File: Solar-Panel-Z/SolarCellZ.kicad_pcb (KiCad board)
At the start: 6 copper layers, 74.1 x 48.4 mm, 62 parts, among them IC1 TSL2561, J1 XF2M-1015-1A, Q1 IRLML2803, U1 NDS8434, U2 Value, U3 Value

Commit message: Finished Cleanup
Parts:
- removed IC1: TSL2561, misc-circuits:TSL2561
- added R17: 0, Resistor_SMD:R_0402_1005Metric, B.Cu at (109.3, 73.9)
- added R18: 0, Resistor_SMD:R_0402_1005Metric, B.Cu at (109.3, 75.8)
- added Ref**: Val**, custom-footprints:ypanel, F.Cu at (118.8, 74.9)
- added TP1: TP, TestPoint:TestPoint_THTPad_D1.0mm_Drill0.5mm, B.Cu at (114.1, 55.3)
- added TP2: TP, TestPoint:TestPoint_THTPad_D1.0mm_Drill0.5mm, B.Cu at (107.9, 55.3)
- added TP3: TP, TestPoint:TestPoint_THTPad_D1.0mm_Drill0.5mm, B.Cu at (110.9, 55.3)
- added TP4: TP, TestPoint:TestPoint_THTPad_D1.0mm_Drill0.5mm, B.Cu at (120.1, 55.3)
- added TP5: TP, TestPoint:TestPoint_THTPad_D1.0mm_Drill0.5mm, B.Cu at (117.3, 55.3)
- D4, D5, R12, R13: moved to B.Cu
- moved D4 58.7 mm to (99.4, 74.1), turned to 0 degrees
- moved R1 57.5 mm to (95.9, 59.3), turned to 180 degrees
- moved D5 56.9 mm to (95.6, 70.2), turned to -90 degrees
- moved C1 56.8 mm to (96.9, 60.3), turned to 180 degrees
- moved R2 55.9 mm to (97.8, 59.3)
- moved SC8 47.7 mm to (85.5, 82.6)
- moved R13 47.5 mm to (108.1, 73.9), turned to -90 degrees
- moved R12 47.3 mm to (108.1, 75.8), turned to -90 degrees
- moved SC2 45.6 mm to (109.6, 45.8), turned to 0 degrees
- moved D3 36.5 mm to (116.3, 72.1), turned to -90 degrees
- moved SC5 30.3 mm to (85.5, 64.2)
- moved SC7 27.0 mm to (85.5, 45.8), turned to 0 degrees
- moved SC6 25.0 mm to (92.8, 73.2)
- moved SC3 18.6 mm to (103.9, 55.2)
- moved SC4 18.1 mm to (109.6, 64.2)
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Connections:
- net /VSOLAR_FULL renamed VSOLAR_FULL
- JP1 pad 1: /coil -> /VBURN
- SC4 pad 1: /coil -> Net-(D3-Pad1)
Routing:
- net VSOLAR_FULL: track 3.25 -> 102.2 mm, vias 0 -> 3
- net Net-(D3-Pad1): track 0.00 -> 72.8 mm, vias 0 -> 4
- net GND: track 6.82 -> 74.2 mm, vias 2 -> 4
- net +3V3: track 2.75 -> 43.8 mm, vias 0 -> 3
- net BATT_P: track 3.63 -> 21.9 mm, vias 0 -> 2
- net SDA1: track 1.09 -> 19.2 mm, vias 1 -> 2
- net SCL1: track 1.13 -> 17.8 mm, vias 1 -> 2
- net /coil: track 15702.4 -> 15688.6 mm, vias 8 -> 7
- net Net-(R10-Pad2): track 3.74 -> 9.89 mm, vias 1 -> 2
- net BURN1: track 22.5 -> 28.3 mm
- net COIL_N: track 15.1 -> 20.1 mm, vias 1 -> 2
- net /VBAT: track 16.1 -> 13.4 mm, vias 3 -> 2
- net Net-(R1-Pad1): track 1.80 -> 4.22 mm
- net VSOLAR: track 1.63 -> 3.99 mm
- net COIL_P: track 17.4 -> 19.6 mm, vias 3 -> 2
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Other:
- board size 74.1 x 48.4 mm -> 48.4 x 48.4 mm
- board text added: "SOLAR_OUT"
- board text added: "v03"
- board text removed: "v02"

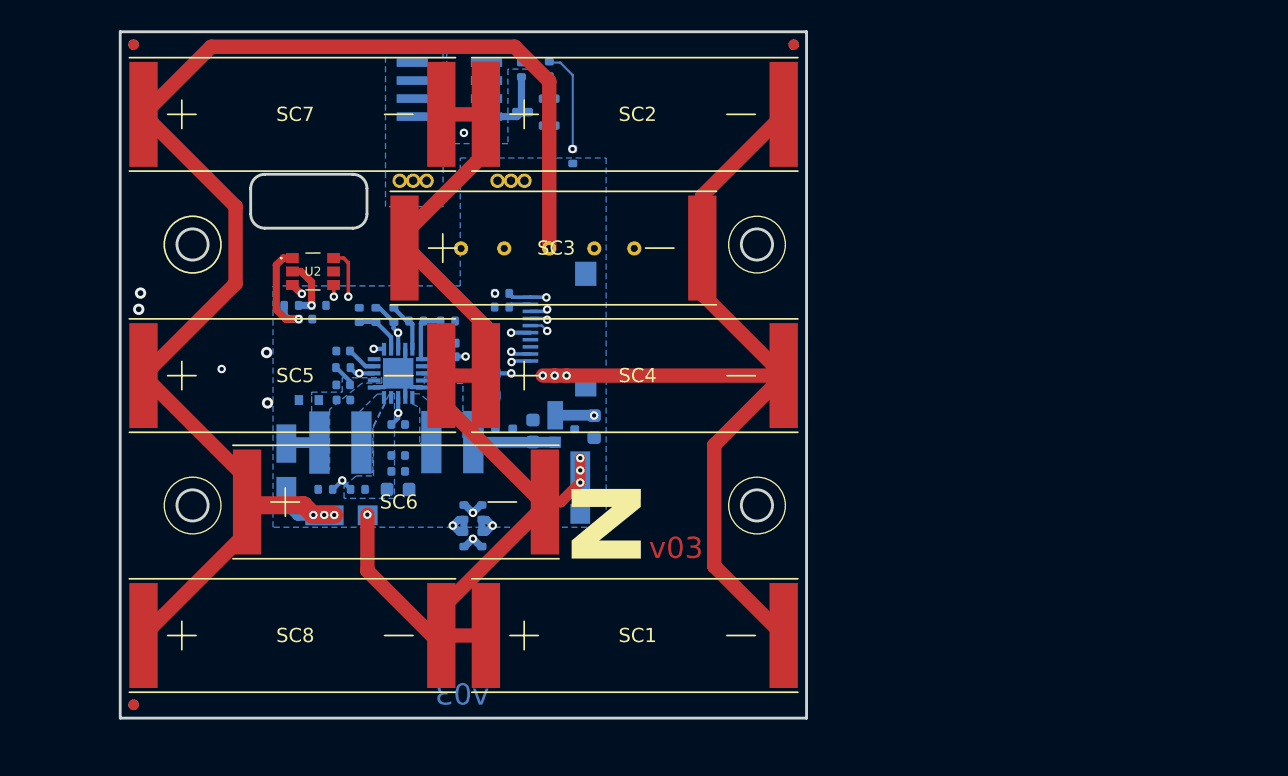
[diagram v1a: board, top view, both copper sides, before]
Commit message: Moved board connectors to North board edges
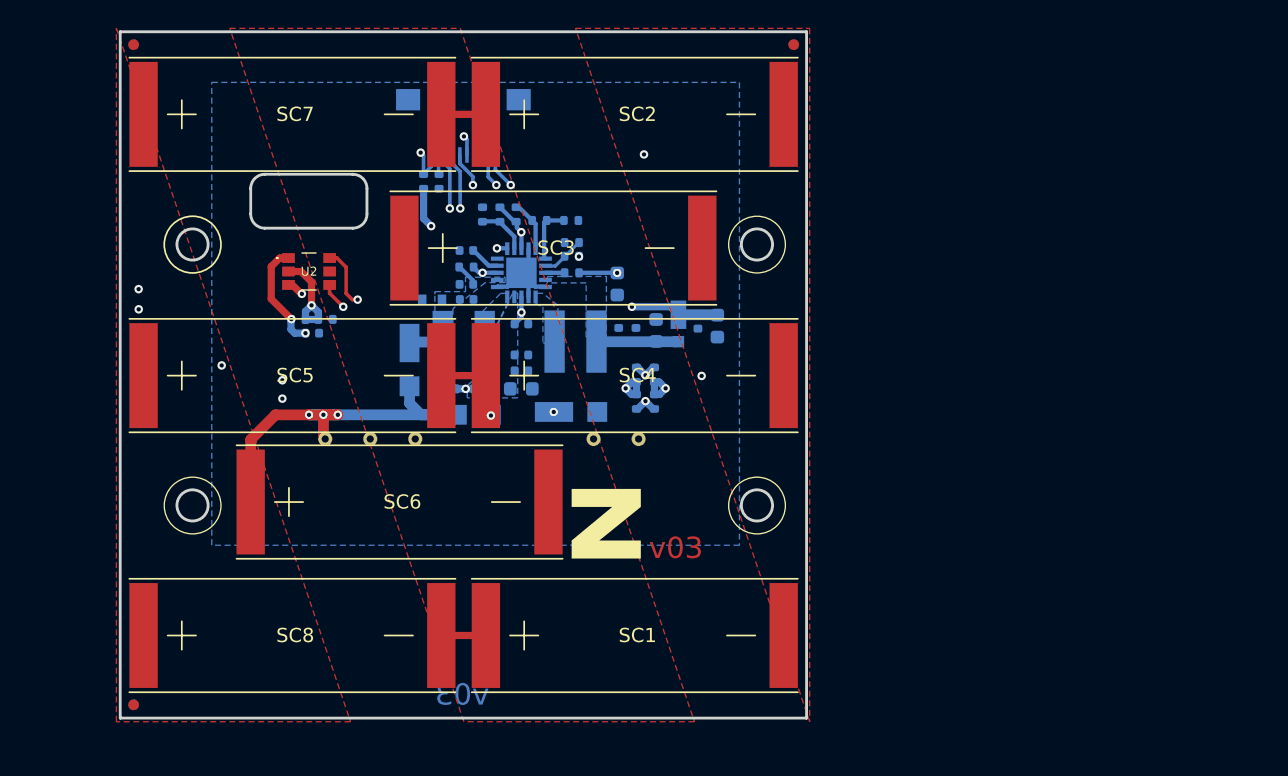
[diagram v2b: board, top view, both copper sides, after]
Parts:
- removed JP1: Jumper, SolarCellParts:Burn-Wire-Rotated
- removed Q1: IRLML2803, Package_TO_SOT_SMD:SOT-23
- removed R19: 100k, Resistor_SMD:R_0402_1005Metric
- removed R3: 10k, Resistor_SMD:R_0402_1005Metric
- removed R4: 4.7k, Resistor_SMD:R_0402_1005Metric
- removed U1: NDS8434, misc-circuits:NDS8434
- added Ref**: Val**, custom-footprints:pycubed_mini_logo, B.Cu at (99.1, 82.4)
- moved TP1 20.7 mm to (98.3, 68.7), turned to 0 degrees
- moved TP5 20.7 mm to (101.5, 68.7), turned to 0 degrees
- moved TP4 20.5 mm to (104.6, 68.7), turned to 0 degrees
- moved TP2 18.4 mm to (120.4, 68.7), turned to 0 degrees
- moved R12 17.8 mm to (121.5, 64.2), turned to 90 degrees
- moved R18 15.9 mm to (120.2, 64.2), turned to -90 degrees
- moved R13 15.5 mm to (121.5, 66.1), turned to 90 degrees
- moved TP3 14.8 mm to (117.2, 68.7), turned to 0 degrees
- moved R17 13.4 mm to (120.2, 66.1), turned to -90 degrees
- moved J1 13.2 mm to (108.0, 48.7), turned to 0 degrees
- moved R5 11.3 mm to (110.6, 52.9)
- moved D2 11.2 mm to (123.2, 60.6)
- moved C11 11.2 mm to (112.1, 65.2)
- moved L2 11.2 mm to (116.0, 61.8)
- moved R15 11.2 mm to (107.0, 65.2)
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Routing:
- net /coil: track 15688.6 -> 15512.4 mm
- net VSOLAR_FULL: track 102.2 -> 27.5 mm
- net GND: track 74.2 -> 8.93 mm, vias 4 -> 3
- net Net-(D3-Pad1): track 72.8 -> 9.43 mm, vias 4 -> 2
- net +3V3: track 43.8 -> 67.3 mm, vias 3 -> 4
- net BURN1: track 28.3 -> 22.1 mm, vias 2 -> 1
- net Net-(Q1-Pad3): track 5.12 -> 0.00 mm
- net COIL_P: track 19.6 -> 24.3 mm
- net BATT_P: track 21.9 -> 26.0 mm, vias 2 -> 1
- net COIL_N: track 20.1 -> 23.3 mm
- net /VBAT: track 13.4 -> 16.2 mm
- net Net-(R1-Pad1): track 4.22 -> 6.85 mm
- net VOUT_EN: track 15.1 -> 12.6 mm
- net Net-(Q1-Pad1): track 1.57 -> 0.00 mm
- net Net-(R10-Pad2): track 9.89 -> 8.35 mm
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- added copper zone on F.Cu, net GND
- added copper zone on F.Cu, net Net-(D3-Pad1)
- added copper zone on F.Cu, net VSOLAR_FULL
- removed copper zone on B.Cu, net /VBURN
- removed copper zone on B.Cu, net BATT_P

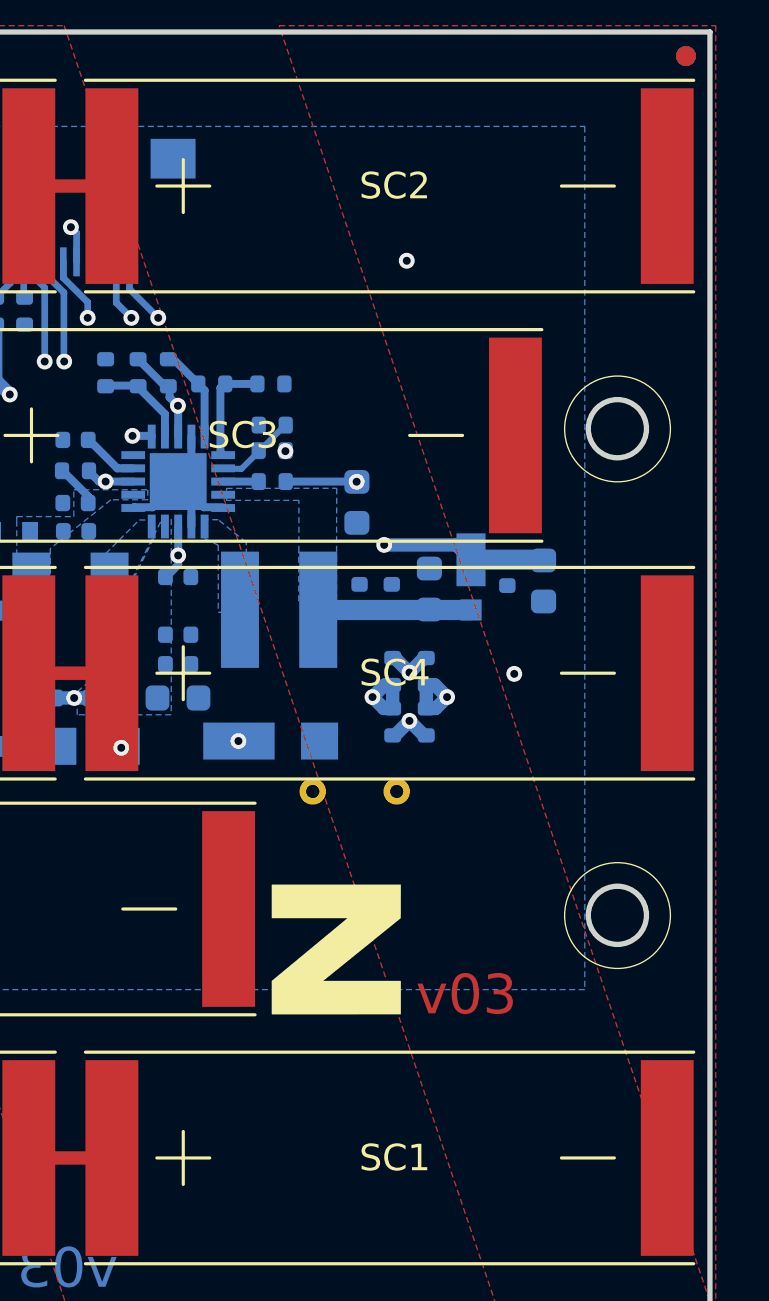
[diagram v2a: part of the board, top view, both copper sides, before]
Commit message: Added JLC order number silkscreen
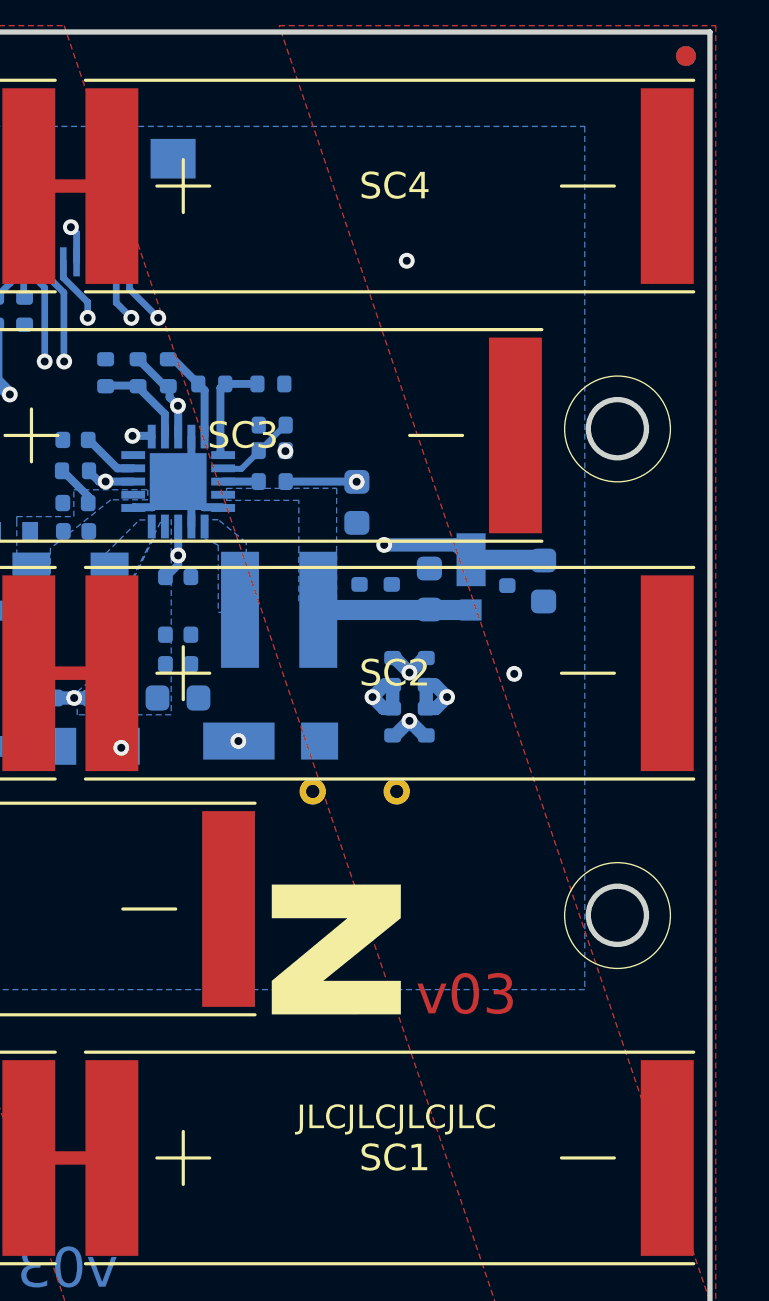
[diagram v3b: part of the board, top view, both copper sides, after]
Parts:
- moved SC4 18.4 mm to (109.6, 45.8)
- moved SC2 18.4 mm to (109.6, 64.2)
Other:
- board text added: "JLCJLCJLCJLC"
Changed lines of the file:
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@@
   )
   (footprint "SolarCellParts:KXOB25-05X3F" (layer "F.Cu")
-    (at 109.62639 45.815809)
+    (at 109.6264 64.2366)
     (property "Sheetfile" "SolarCellZ.kicad_sch")
     (property "Sheetname" "")
@@
   )
   (footprint "SolarCellParts:KXOB25-05X3F" (layer "F.Cu")
-    (at 109.6264 64.2366)
+    (at 109.6264 45.815783)
     (property "Sheetfile" "SolarCellZ.kicad_sch")
     (property "Sheetname" "")
@@
     (effects (font (size 0.762 0.762) (thickness 0.127)) (justify mirror))
   )
+  (gr_text "JLCJLCJLCJLC" (at 120.396 81.026) (layer "F.SilkS")
+    (effects (font (size 0.889 0.889) (thickness 0.15)))
+  )
   (gr_text "v03\n" (at 107.95 86.741) (layer "B.Mask")
